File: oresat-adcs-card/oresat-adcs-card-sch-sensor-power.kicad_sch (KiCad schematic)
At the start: 84 parts, among them Q26 MOSFET-PCH-SOT23-6, Q27 MOSFET-PCH-SOT23-6, Q28 PMV45EN2R, Q29 PMV45EN2R, Q30 MOSFET-PCH-dual-SOT23-6, U29 MAX7310ATE, U30 MAX4211FETE, U31 TPS62111RSA, U32 MIC842LYC5-TR, U33 MIC842LYC5-TR, U41 TS5A21366DCUR

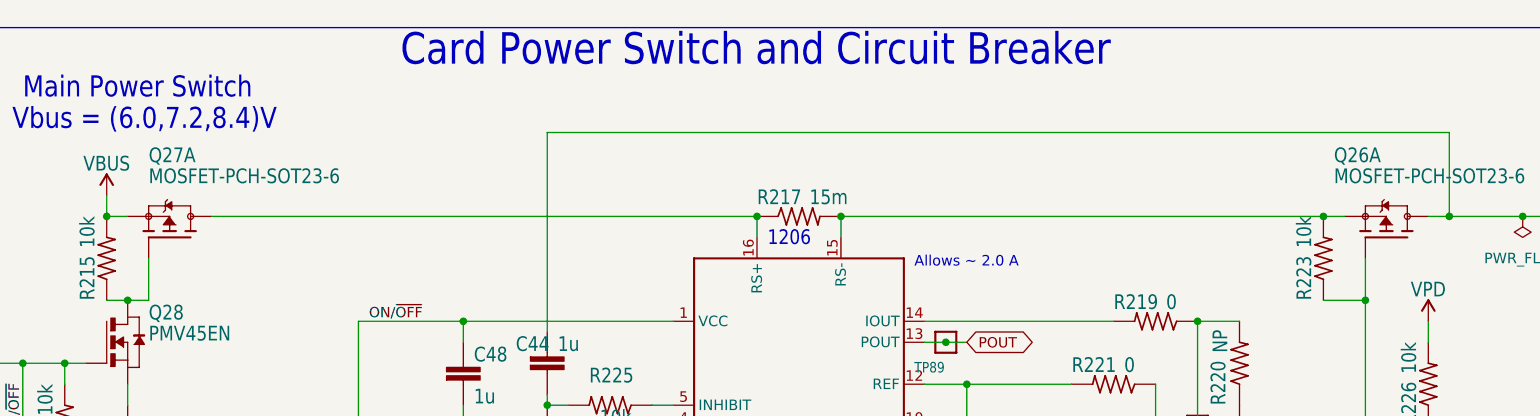
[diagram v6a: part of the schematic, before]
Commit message: Updated ADCS card and fixed library issues
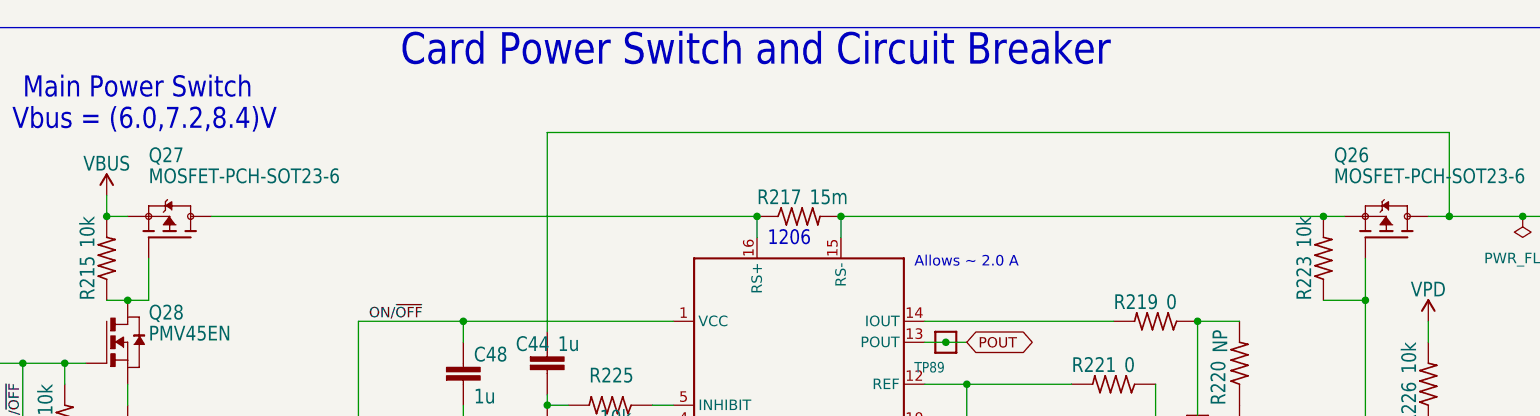
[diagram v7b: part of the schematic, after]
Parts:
- C43, C44, C46, C48, C49, C50, C99, R122, R123, R124, R198, R199, R200, R201, R202, R203, R204, R205, R206, R207, R208, R209, R210, R211, R212, R213, R214, R215, R216, R218, R219, R220, R221, R222, R223, R224, R225, R226, R227, R228, R267, R268, R269, R270, R271, R272, R273, R274: footprint oresat-acs-card:.0603-C-NOSILK -> oresat-passives:0603-C-NOSILK
- C45, C47: footprint oresat-acs-card:.0805-B-NOSILK -> oresat-passives:0805-B-NOSILK

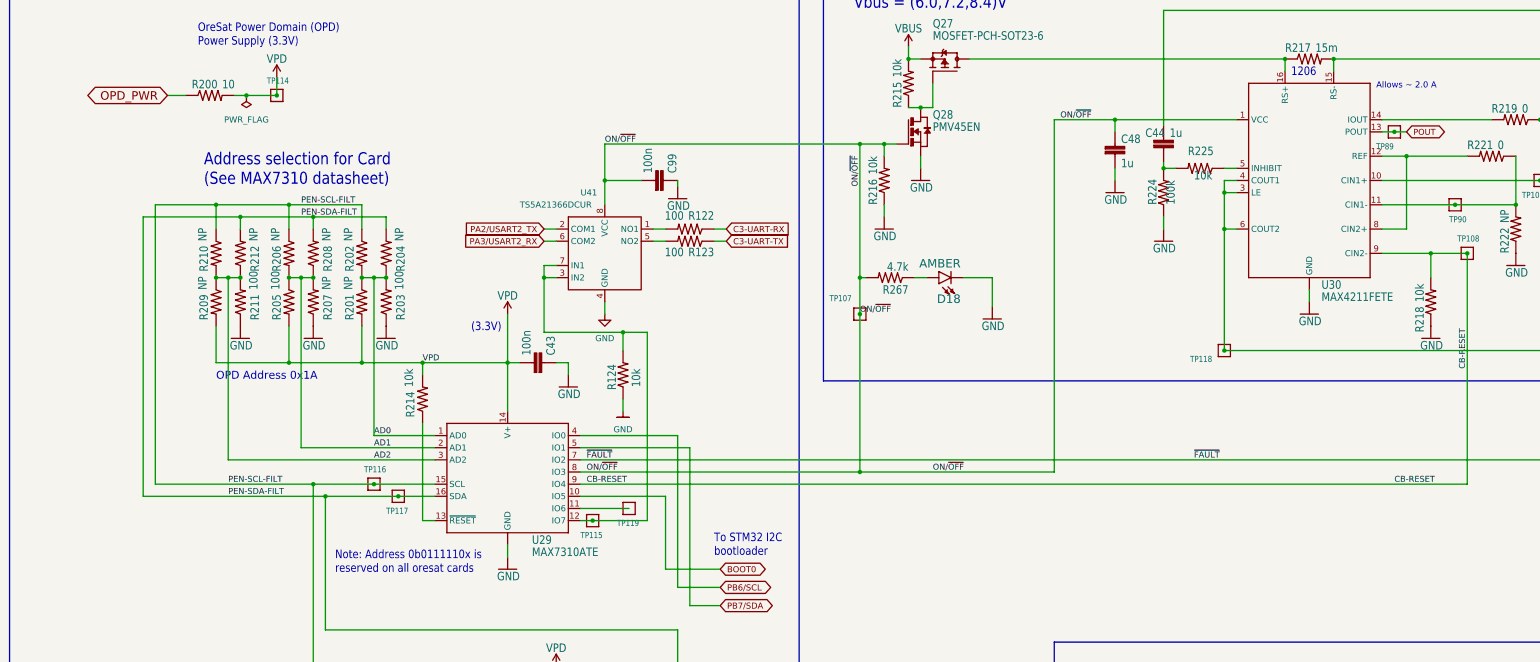
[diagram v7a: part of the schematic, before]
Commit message: Design review changes
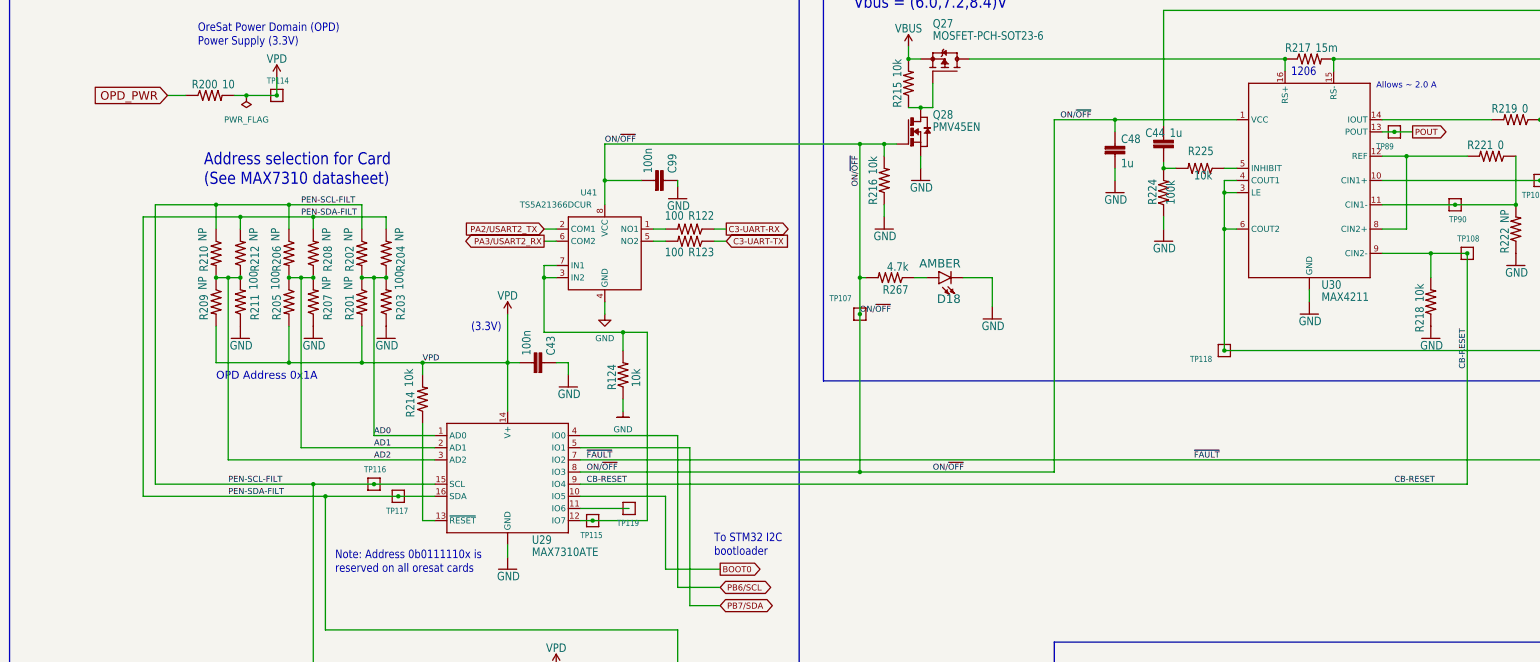
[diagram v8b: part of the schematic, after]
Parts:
- U30: value MAX4211FETE -> MAX4211
- U32, U33: value MIC842LYC5-TR -> MIC842LYC5
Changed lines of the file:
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@@
   (junction (at 303.53 38.1) (diameter 0) (color 0 0 0 0)
   )
+  (junction (at 316.23 53.34) (diameter 0) (color 0 0 0 0)
+  )
   (junction (at 140.97 212.09) (diameter 0) (color 0 0 0 0)
   )
@@
   (junction (at 76.2 45.72) (diameter 0) (color 0 0 0 0)
   )
-  (junction (at 316.23 53.34) (diameter 0) (color 0 0 0 0)
-  )
   (junction (at 118.11 224.79) (diameter 0) (color 0 0 0 0)
   )
@@
     (stroke (width 0) (type default))
   )
-  (wire (pts (xy 316.23 53.34) (xy 318.77 53.34))
-    (stroke (width 0) (type default))
-  )
   (wire (pts (xy 107.95 224.79) (xy 102.87 224.79))
     (stroke (width 0) (type default))
@@
   )
   (wire (pts (xy 100.33 101.6) (xy 113.03 101.6))
+    (stroke (width 0) (type default))
+  )
+  (wire (pts (xy 316.23 53.34) (xy 320.04 53.34))
     (stroke (width 0) (type default))
   )
@@
     (effects (font (size 1.2446 1.2446)) (justify left bottom))
   )
-  (global_label "PA3{slash}USART2_RX" (shape input) (at 138.43 76.2 180) (fields_autoplaced)
+  (global_label "PA3{slash}USART2_RX" (shape output) (at 138.43 76.2 180) (fields_autoplaced)
     (effects (font (size 1.27 1.27)) (justify right))
-    (property "Intersheetrefs" "${INTERSHEET_REFS}" (at 120.5955 76.2794 0)
-      (effects (font (size 1.27 1.27)) (justify right) hide)
-    )
-  )
-  (global_label "C3-UART-RX" (shape input) (at 176.53 73.66 0) (fields_autoplaced)
+    (property "Intersheetrefs" "${INTERSHEET_REFS}" (at 120.1028 76.2 0)
+      (effects (font (size 1.27 1.27)) (justify right))
+    )
+  )
+  (global_label "C3-UART-RX" (shape output) (at 176.53 73.66 0) (fields_autoplaced)
     (effects (font (size 1.27 1.27)) (justify left))
-    (property "Intersheetrefs" "${INTERSHEET_REFS}" (at 191.7036 73.5806 0)
-      (effects (font (size 1.27 1.27)) (justify left) hide)
+    (property "Intersheetrefs" "${INTERSHEET_REFS}" (at 192.1963 73.66 0)
+      (effects (font (size 1.27 1.27)) (justify left))
     )
   )
@@
     (effects (font (size 1.778 1.778)) (justify right))
     (property "Intersheetrefs" "${INTERSHEET_REFS}" (at 95.25 -210.82 0)
-      (effects (font (size 1.27 1.27)) hide)
+      (effects (font (size 1.27 1.27)))
     )
   )
   (global_label "PA2{slash}USART2_TX" (shape input) (at 138.43 73.66 180) (fields_autoplaced)
     (effects (font (size 1.27 1.27)) (justify right))
-    (property "Intersheetrefs" "${INTERSHEET_REFS}" (at 120.8979 73.5806 0)
-      (effects (font (size 1.27 1.27)) (justify right) hide)
+    (property "Intersheetrefs" "${INTERSHEET_REFS}" (at 120.4052 73.66 0)
+      (effects (font (size 1.27 1.27)) (justify right))
     )
   )
   (global_label "C3-UART-TX" (shape input) (at 176.53 76.2 0) (fields_autoplaced)
     (effects (font (size 1.27 1.27)) (justify left))
-    (property "Intersheetrefs" "${INTERSHEET_REFS}" (at 191.4012 76.1206 0)
-      (effects (font (size 1.27 1.27)) (justify left) hide)
-    )
-  )
-  (global_label "POUT" (shape bidirectional) (at 318.77 53.34 0) (fields_autoplaced)
-    (effects (font (size 1.2446 1.2446)) (justify left))
-    (property "Intersheetrefs" "${INTERSHEET_REFS}" (at -8.89 -12.7 0)
-      (effects (font (size 1.27 1.27)) hide)
+    (property "Intersheetrefs" "${INTERSHEET_REFS}" (at 191.8939 76.2 0)
+      (effects (font (size 1.27 1.27)) (justify left))
     )
   )
@@
     (effects (font (size 1.27 1.27)) (justify left))
     (property "Intersheetrefs" "${INTERSHEET_REFS}" (at 186.3212 152.3206 0)
-      (effects (font (size 1.27 1.27)) (justify left) hide)
+      (effects (font (size 1.27 1.27)) (justify left))
     )
   )
@@
     (effects (font (size 1.778 1.778)) (justify right))
     (property "Intersheetrefs" "${INTERSHEET_REFS}" (at 95.25 -121.92 0)
-      (effects (font (size 1.27 1.27)) hide)
+      (effects (font (size 1.27 1.27)))
     )
   )
@@
     (effects (font (size 1.27 1.27)) (justify left))
     (property "Intersheetrefs" "${INTERSHEET_REFS}" (at 186.2607 148.5106 0)
-      (effects (font (size 1.27 1.27)) (justify left) hide)
-    )
-  )
-  (global_label "BOOT0" (shape bidirectional) (at 175.26 144.78 0) (fields_autoplaced)
+      (effects (font (size 1.27 1.27)) (justify left))
+    )
+  )
+  (global_label "POUT" (shape output) (at 320.04 53.34 0) (fields_autoplaced)
     (effects (font (size 1.27 1.27)) (justify left))
-    (property "Intersheetrefs" "${INTERSHEET_REFS}" (at 183.7812 144.7006 0)
-      (effects (font (size 1.27 1.27)) (justify left) hide)
-    )
-  )
-  (global_label "OPD_PWR" (shape bidirectional) (at 59.69 45.72 180) (fields_autoplaced)
+    (property "Intersheetrefs" "${INTERSHEET_REFS}" (at 327.8444 53.34 0)
+      (effects (font (size 1.27 1.27)) (justify left))
+    )
+  )
+  (global_label "BOOT0" (shape output) (at 175.26 144.78 0) (fields_autoplaced)
+    (effects (font (size 1.27 1.27)) (justify left))
+    (property "Intersheetrefs" "${INTERSHEET_REFS}" (at 184.2739 144.78 0)
+      (effects (font (size 1.27 1.27)) (justify left))
+    )
+  )
+  (global_label "OPD_PWR" (shape input) (at 59.69 45.72 180) (fields_autoplaced)
     (effects (font (size 1.778 1.778)) (justify right))
-    (property "Intersheetrefs" "${INTERSHEET_REFS}" (at 92.71 -490.22 0)
-      (effects (font (size 1.27 1.27)) hide)
+    (property "Intersheetrefs" "${INTERSHEET_REFS}" (at 43.2608 45.72 0)
+      (effects (font (size 1.27 1.27)) (justify right))
     )
   )
@@
       (effects (font (size 1.27 1.27)) hide)
     )
-    (property "Value" "MIC842LYC5-TR" (at 140.97 182.88 0)
+    (property "Value" "MIC842LYC5" (at 140.97 182.88 0)
       (effects (font (size 1.27 1.0795)) (justify left bottom) hide)
     )
@@
     (pin "4")
     (pin "5")
+    (pin "3")
     (instances
       (project "oresat-adcs-card"
@@
       (effects (font (size 1.778 1.5113)) (justify left bottom))
     )
-    (property "Value" "MAX4211FETE" (at 300.99 88.9 0)
+    (property "Value" "MAX4211" (at 300.99 88.9 0)
       (effects (font (size 1.778 1.5113)) (justify left bottom))
     )
@@
       (effects (font (size 1.27 1.27)) hide)
     )
-    (property "Value" "MAX4211FETE" (at 298.45 60.96 0)
+    (property "Value" "MAX4211" (at 298.45 60.96 0)
       (effects (font (size 1.778 1.5113)) (justify left bottom) hide)
     )
@@
     (pin "9")
     (pin "EPAD")
+    (pin "2")
     (instances
       (project "oresat-adcs-card"
@@
       (effects (font (size 1.27 1.27)) hide)
     )
-    (property "Value" "MIC842LYC5-TR" (at 140.97 227.33 0)
+    (property "Value" "MIC842LYC5" (at 140.97 227.33 0)
       (effects (font (size 1.27 1.0795)) (justify left bottom) hide)
     )
@@
     (pin "4")
     (pin "5")
-    (instances
-      (project "oresat-adcs-card"
+    (pin "3")
+    (instances
+      (project "oresat-adcs-card"
